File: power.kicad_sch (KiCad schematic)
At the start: 44 parts, among them IC1 MP9943AGQ-Z, IC2 MP9943AGQ-Z, U10 MAX40200ANS_T, U11 MAX40200ANS_T, U4 AP2112K-3.3TRG1, U5 AP2112K-1.8TRG1

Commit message: routing...
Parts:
- IC1, IC2: footprint fcg4_fp:SON65P300X300X100-8M -> SON65P300X300X100-8M
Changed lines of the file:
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@@
 			)
 		)
-		(property "Footprint" "fcg4_fp:SON65P300X300X100-8M"
+		(property "Footprint" "SON65P300X300X100-8M"
 			(at 217.17 185.09 0)
 			(effects
@@
 			)
 		)
-		(property "Footprint" "fcg4_fp:SON65P300X300X100-8M"
+		(property "Footprint" "SON65P300X300X100-8M"
 			(at 85.09 183.82 0)
 			(effects

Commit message: routing
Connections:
- net VOUT renamed VCC_ICM
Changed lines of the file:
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@@
+	)
+	(junction
+		(at 238.76 35.56)
+		(diameter 0)
+		(color 0 0 0 0)
 	)
 	(junction
@@
 	(wire
 		(pts
+			(xy 238.76 35.56) (xy 240.03 35.56)
+		)
+		(stroke
+			(width 0)
+			(type default)
+		)
+	)
+	(wire
+		(pts
 			(xy 72.39 34.29) (xy 72.39 41.91)
 		)
@@
 	(label "EN{slash}SYNC_5V5"
 		(at 45.72 93.98 0)
-		(effects
-			(font
-				(size 1.27 1.27)
-			)
-			(justify left bottom)
-		)
-	)
-	(label "VOUT"
-		(at 234.95 35.56 0)
 		(effects
 			(font
@@
 				(hide yes)
 			)
+		)
+	)
+	(global_label "VCC_ICM"
+		(shape input)
+		(at 240.03 35.56 0)
+		(fields_autoplaced yes)
+		(effects
+			(font
+				(size 1.27 1.27)
+			)
+			(justify left)
+		)
+		(property "Intersheetrefs" "${INTERSHEET_REFS}"
+			(at 250.9376 35.56 0)
+			(effects
+				(font
+					(size 1.27 1.27)
+				)
+				(justify left)
+				(hide yes)
+			)

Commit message: Update component properties in schematics with manufacturer details and datasheets
- Added manufacturer name, part number, and LCSC part name for various components in mcu.kicad_sch, power.kicad_sch, and sensor.kicad_sch.
- Updated datasheet links for components to point to the correct URLs.
- Ensured all new properties are hidden in the schematic view.
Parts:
- C1, C2, C20, C21, C35, C41: LCSC Part Name (none) -> C1518208; Manufacturer_Name (none) -> muRata; Manufacturer_Part_Number (none) -> GRM155R61H105KE05D
- C23, C31, C36, C37: LCSC Part Name (none) -> C77020; Manufacturer_Name (none) -> muRata; Manufacturer_Part_Number (none) -> GRM155R71H104KE14D

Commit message: Almost completed! Update component properties in sensor schematic
- Added datasheets, LCSC part names, manufacturer names, and manufacturer part numbers for various components in the sensor.kicad_sch file.
- Updated the datasheet links for components to point to the correct URLs.
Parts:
- C16, C17, C18, C19: footprint Capacitor_SMD:C_0603_1608Metric -> Capacitor_SMD:C_0805_2012Metric; LCSC Part Name (none) -> C403725; Manufacturer_Name (none) -> muRata; Manufacturer_Part_Number (none) -> GRM31CR61E476ME44L
- C22, C34, C38, C39: footprint Capacitor_SMD:C_0402_1005Metric -> Capacitor_SMD:C_0603_1608Metric; LCSC Part Name (none) -> C194427; Manufacturer_Name (none) -> muRata; Manufacturer_Part_Number (none) -> GRM188R6YA106MA73D
- C32, C33, C40, C42: LCSC Part Name (none) -> C29519229; Manufacturer_Name (none) -> muRata; Manufacturer_Part_Number (none) -> GRM188C61E226ME01D
- L1, L2: footprint Inductor_SMD:L_0603_1608Metric -> Inductor_SMD:L_1210_3225Metric; LCSC Part Name (none) -> C39846661; Manufacturer_Name (none) -> XR; Manufacturer_Part_Number LQM18DH100M70L -> XRTC322512S100MBCA
- R1: LCSC Part Name (none) -> C155695; Manufacturer_Name (none) -> YAGEO; Manufacturer_Part_Number (none) -> RC0402FR-077K68L
- R16, R19: LCSC Part Name (none) -> C138033; Manufacturer_Name (none) -> YAGEO; Manufacturer_Part_Number (none) -> RC0402FR-071ML
- R17, R21: LCSC Part Name (none) -> C138031; Manufacturer_Name (none) -> YAGEO; Manufacturer_Part_Number (none) -> RC0402FR-0720RL
- R18, R20: LCSC Part Name (none) -> C60491; Manufacturer_Name (none) -> YAGEO; Manufacturer_Part_Number (none) -> RC0402FR-07100KL
- R2, R6: LCSC Part Name (none) -> C26978; Manufacturer_Name (none) -> UNI-ROYAL; Manufacturer_Part_Number (none) -> 0402WGF4122TCE
- R3, R4: LCSC Part Name (none) -> C107229; Manufacturer_Name (none) -> YAGEO; Manufacturer_Part_Number (none) -> RC0402FR-0751KL
- R5: LCSC Part Name (none) -> C137988; Manufacturer_Name (none) -> YAGEO; Manufacturer_Part_Number (none) -> RC0402FR-073K92L
- R7: LCSC Part Name (none) -> C60490; Manufacturer_Name (none) -> YAGEO; Manufacturer_Part_Number (none) -> RC0402FR-0710KL
- R8: LCSC Part Name (none) -> C106235; Manufacturer_Name (none) -> YAGEO; Manufacturer_Part_Number (none) -> RC0402FR-071KL
- U10, U11: Manufacturer_Name (none) -> Analog Devices / Maxim Integrated; Manufacturer_Part_Number (none) -> MAX40200ANS+T; Mouser Part Number (none) -> 700-MAX40200ANS+T
- U4: Manufacturer_Name (none) -> Diodes Incorporated; Manufacturer_Part_Number (none) -> AP2112K-3.3TRG1; Mouser Part Number (none) -> 621-AP2112K-3.3TRG1
- U5: Manufacturer_Name (none) -> Diodes Incorporated; Manufacturer_Part_Number (none) -> AP2112K-1.8TRG1; Mouser Part Number (none) -> 621-AP2112K-1.8TRG1

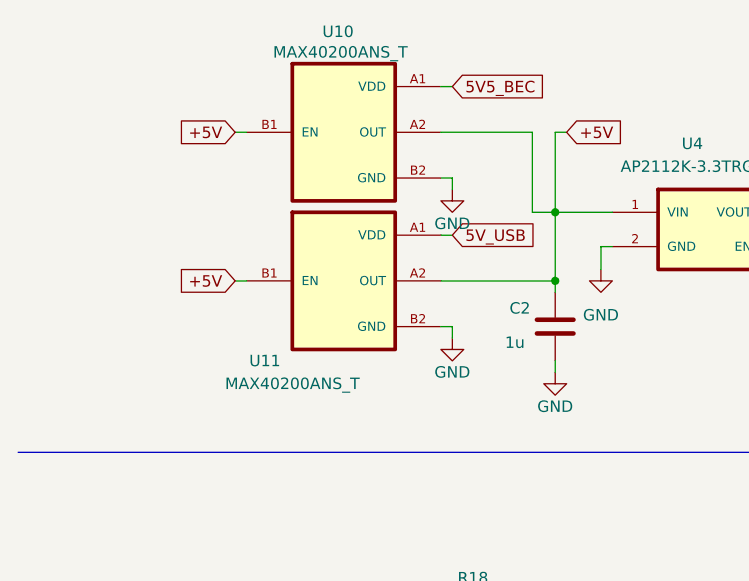
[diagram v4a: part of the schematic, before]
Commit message: Add Availability and Price properties to multiple components in schematic
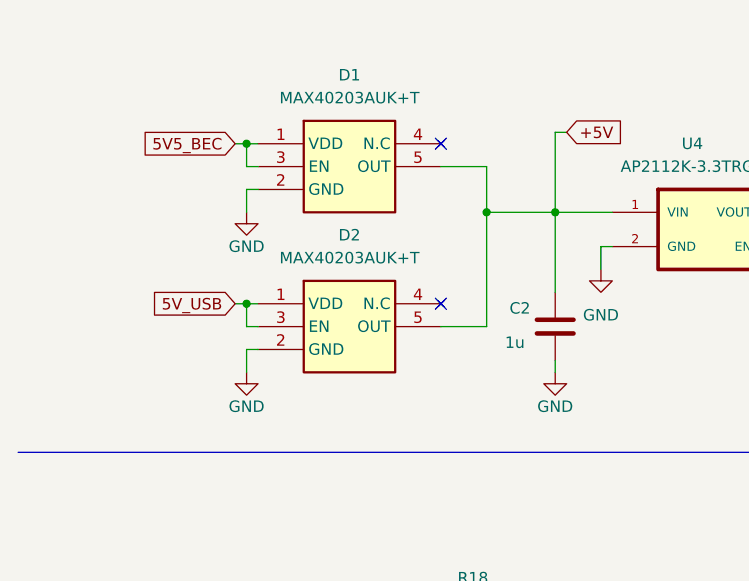
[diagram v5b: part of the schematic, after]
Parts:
- removed U10, U11: MAX40200ANS_T, fcg4_fp:BGA4N35P2X2_72X72X50N, symbol fcg4:MAX40200ANS_T
- added D1, D2: MAX40203AUK+T, fcg4_fp:SOT95P280X145-5M, symbol fcg4:MAX40203AUK+T
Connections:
- net +5V: now also D1.5 (OUT), D2.5 (OUT)
- net 5V5_BEC: now also D1.1 (VDD), D1.3 (EN)
- net 5V_USB: now also D2.1 (VDD), D2.3 (EN)
- net GND: now also D1.2 (GND), D2.2 (GND)
- no-connect marks 3 -> 5

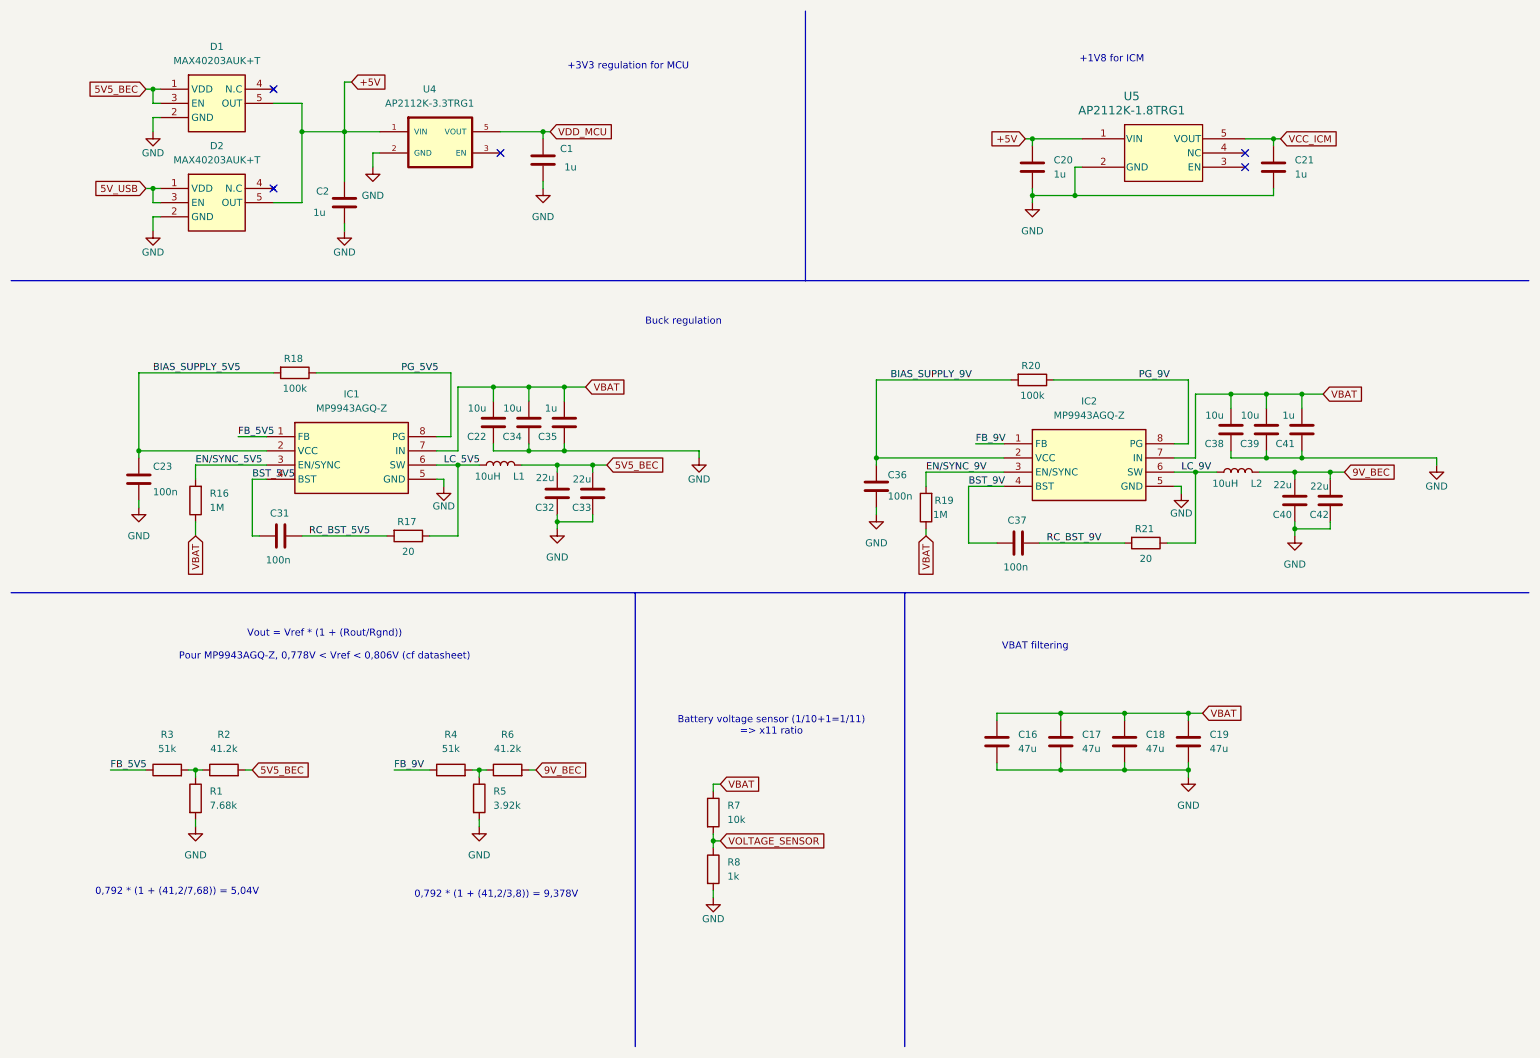
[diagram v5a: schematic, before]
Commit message: update buck regulator to a more recent one
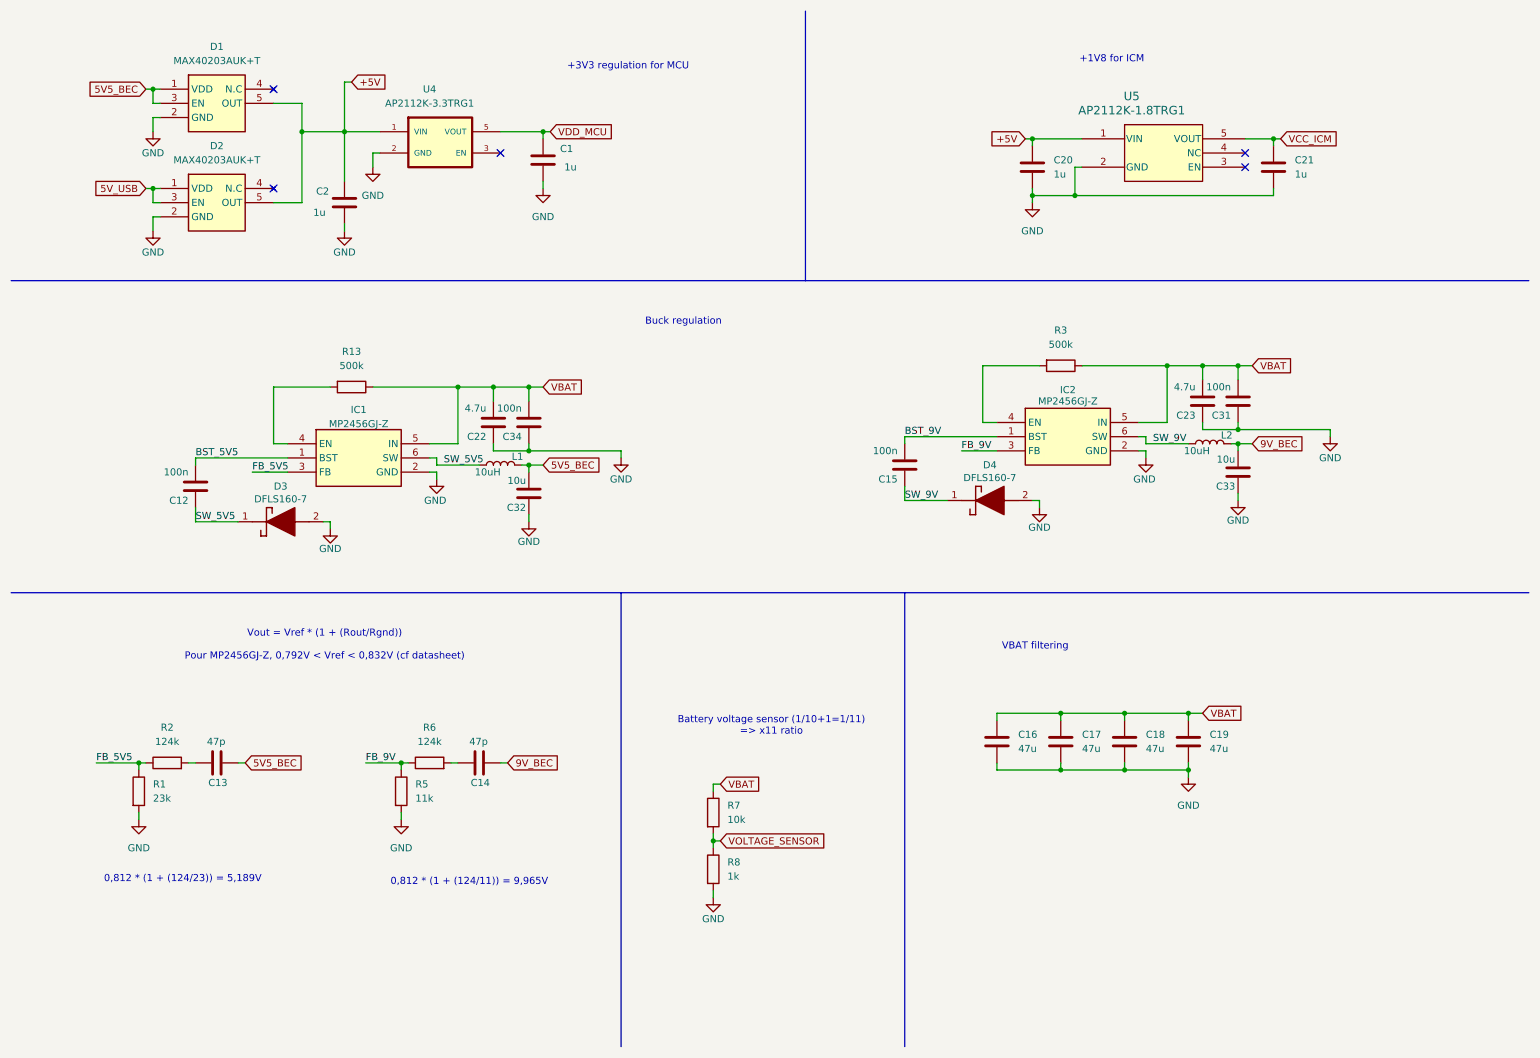
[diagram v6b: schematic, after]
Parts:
- removed C35, C41: 1u, Capacitor_SMD:C_0402_1005Metric, symbol Device:C
- removed C36, C37: 100n, Capacitor_SMD:C_0402_1005Metric, symbol Device:C
- removed C38, C39: 10u, Capacitor_SMD:C_0603_1608Metric, symbol Device:C
- removed C40, C42: 22u, Capacitor_SMD:C_0603_1608Metric, symbol Device:C
- removed IC1, IC2: MP9943AGQ-Z, SON65P300X300X100-8M, symbol fcg4:MP9943AGQ-Z
- removed R16, R19: 1M, Resistor_SMD:R_0402_1005Metric, symbol Device:R
- removed R17, R21: 20, Resistor_SMD:R_0402_1005Metric, symbol Device:R
- removed R18, R20: 100k, Resistor_SMD:R_0402_1005Metric, symbol Device:R
- removed R4: 51k, Resistor_SMD:R_0402_1005Metric, symbol Device:R
- added C12, C15: 100n, Capacitor_SMD:C_0402_1005Metric, symbol Device:C
- added C13: 47p, Capacitor_SMD:C_0402_1005Metric, symbol Device:C
- added C14: 47p, Capacitor_SMD:C_0603_1608Metric, symbol Device:C
- added D3, D4: DFLS160-7, fcg4_fp:DFLS1607, symbol fcg4:DFLS160-7
- added IC1, IC2: MP2456GJ-Z, fcg4_fp:SOP95P280X100-6M, symbol fcg4:MP2456GJ-Z
- added R13: 500k, Resistor_SMD:R_0402_1005Metric, symbol Device:R
- C22: value 10u -> 4.7u
- C23: value 100n -> 4.7u; footprint Capacitor_SMD:C_0402_1005Metric -> Capacitor_SMD:C_0603_1608Metric; LCSC Part Name C77020 -> C194427; Manufacturer_Part_Number GRM155R71H104KE14D -> GRM188R6YA106MA73D
- C31: LCSC Part Name C77020 -> C194427; Manufacturer_Part_Number GRM155R71H104KE14D -> GRM188R6YA106MA73D
- C32, C33: value 22u -> 10u
- C34: value 10u -> 100n; footprint Capacitor_SMD:C_0603_1608Metric -> Capacitor_SMD:C_0402_1005Metric
- R1: value 7.68k -> 23k
- R2, R6: value 41.2k -> 124k
- R3: value 51k -> 500k; LCSC Part Name C107229 -> C138033; Manufacturer_Part_Number RC0402FR-0751KL -> RC0402FR-071ML
- R5: value 3.92k -> 11k
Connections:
- net BIAS_SUPPLY_5V5 is gone; now on net GND: C23.1
- net RC_BST_5V5 is gone; now on net VBAT: C31.2
- net 5V5_BEC: now also C13.1; no longer C33.2, R2.2
- net 9V_BEC: now also C33.2, C14.1; no longer R6.2
- net BST_5V5: now also C12.2, IC1.1 (BST); no longer C31.1
- net BST_9V: now also C15.2, IC2.1 (BST)
- net FB_5V5: now also R1.1, R2.1, IC1.3 (FB); no longer R3.1
- net FB_9V: now also R5.1, R6.1, IC2.3 (FB)
- net GND: now also C31.1, D3.2 (A), D4.2 (A), IC1.2 (GND), IC2.2 (GND); no longer C23.2
- net VBAT: now also C23.2, R3.1, IC1.5 (IN), IC2.5 (IN), R13.1
- net LC_5V5 renamed SW_5V5
- net SW_5V5: now also C12.1, D3.1 (K), IC1.6 (SW)
- net LC_9V renamed SW_9V
- net SW_9V: now also C15.1, D4.1 (K), IC2.6 (SW)
- new net: IC2.4 (EN), R3.2
- new net: C14.2, R6.2
- new net: C13.2, R2.2
- new net: IC1.4 (EN), R13.2
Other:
- note added: "0,812 * (1 + (124/11)) = 9,965V"
- note added: "0,812 * (1 + (124/23)) = 5,189V"
- note added: "Vout = Vref * (1 + (Rout/Rgnd)) Pour MP2456GJ-Z, 0,792V < Vref < 0,832V (cf datasheet)"
- note removed: "0,792 * (1 + (41,2/3,8)) = 9,378V"
- note removed: "0,792 * (1 + (41,2/7,68)) = 5,04V"
- note removed: "Vout = Vref * (1 + (Rout/Rgnd)) Pour MP9943AGQ-Z, 0,778V < Vref < 0,806V (cf datasheet)"
- moved on the sheet: C32, R1, R2, R5, R6
